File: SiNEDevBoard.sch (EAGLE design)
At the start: 37 parts, among them IC1 ATTINY24/44/84-SSU, IC2 74HC164D, J1 AVR_SPI_PRG_6NS

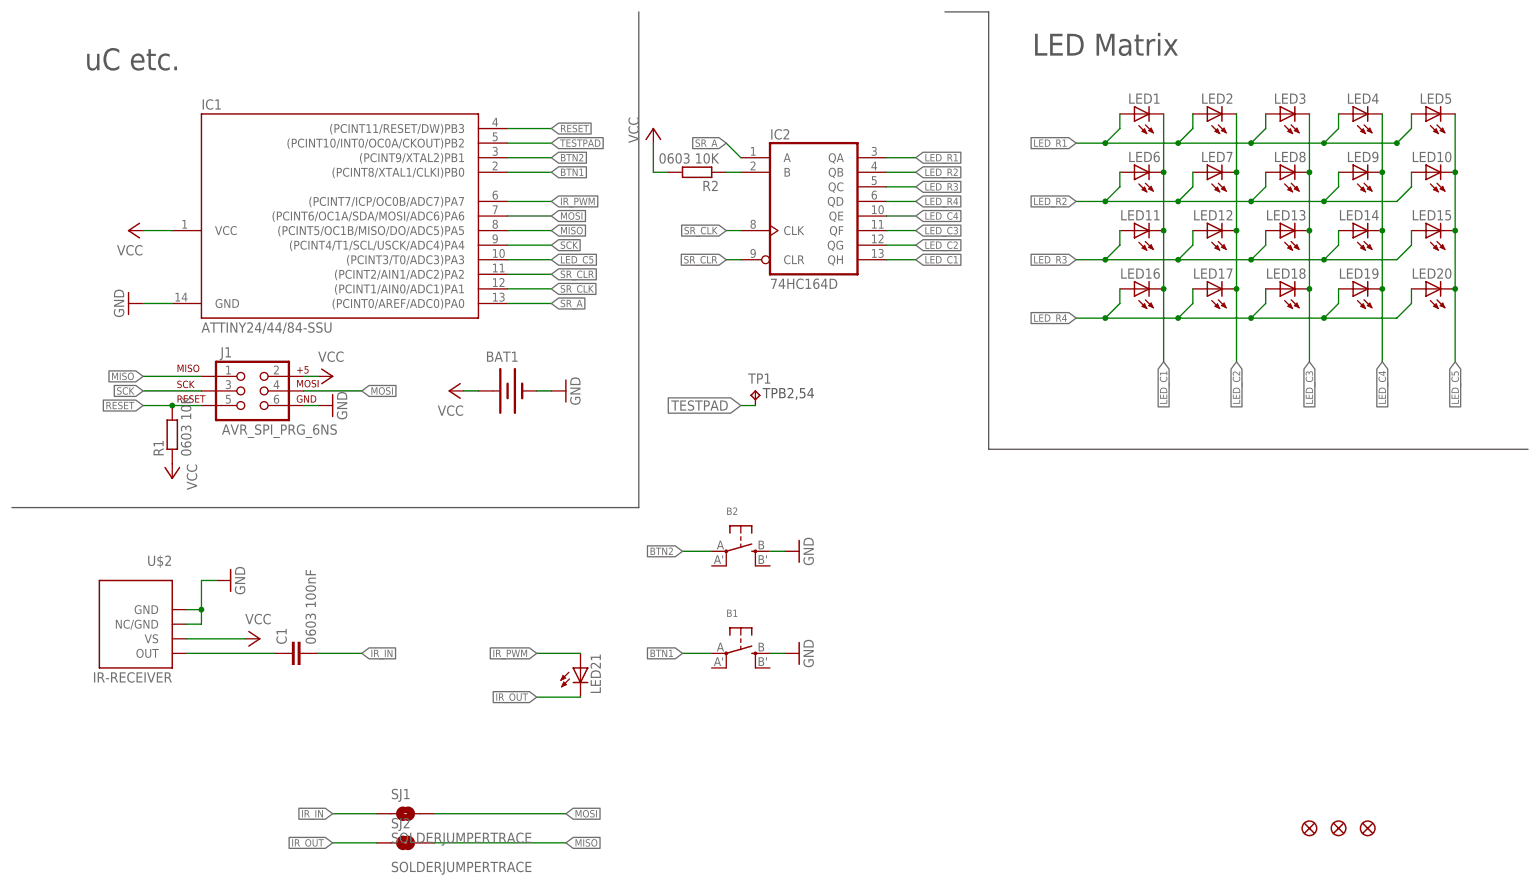
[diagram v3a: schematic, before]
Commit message: DevBoard V0.5 Final Changes including Teardrops, this version was sent to make 3 prototype boards
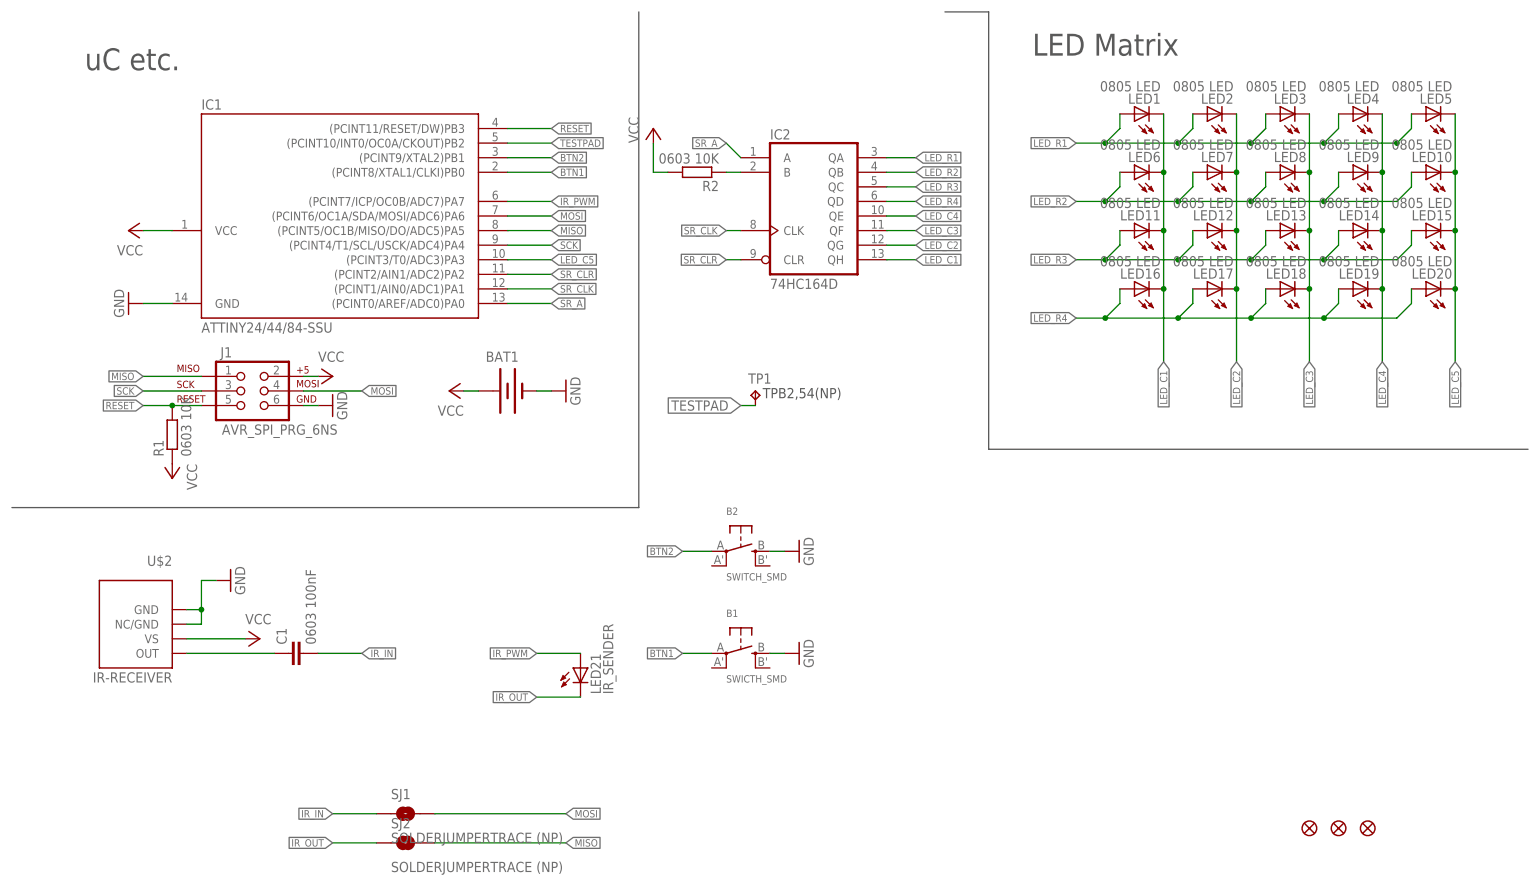
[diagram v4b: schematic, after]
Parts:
- B1: value (none) -> SWICTH_SMD
- B2: value (none) -> SWITCH_SMD
- LED1, LED10, LED11, LED12, LED13, LED14, LED15, LED16, LED17, LED18, LED19, LED2, LED20, LED3, LED4, LED5, LED6, LED7, LED8, LED9: value (none) -> 0805 LED
- LED21: value (none) -> IR_SENDER
- SJ1, SJ2: value SOLDERJUMPERTRACE -> SOLDERJUMPERTRACE (NP)
- TP1: value TPB2,54 -> TPB2,54(NP)
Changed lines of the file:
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@@
 <part name="GND3" library="supply1" deviceset="GND" device=""/>
 <part name="P+4" library="supply1" deviceset="VCC" device=""/>
-<part name="LED1" library="adafruit" deviceset="LED" device="CHIPLED_0805"/>
-<part name="LED2" library="adafruit" deviceset="LED" device="CHIPLED_0805"/>
-<part name="LED3" library="adafruit" deviceset="LED" device="CHIPLED_0805"/>
-<part name="LED4" library="adafruit" deviceset="LED" device="CHIPLED_0805"/>
-<part name="LED5" library="adafruit" deviceset="LED" device="CHIPLED_0805"/>
-<part name="LED6" library="adafruit" deviceset="LED" device="CHIPLED_0805"/>
-<part name="LED7" library="adafruit" deviceset="LED" device="CHIPLED_0805"/>
-<part name="LED8" library="adafruit" deviceset="LED" device="CHIPLED_0805"/>
-<part name="LED9" library="adafruit" deviceset="LED" device="CHIPLED_0805"/>
-<part name="LED10" library="adafruit" deviceset="LED" device="CHIPLED_0805"/>
-<part name="LED11" library="adafruit" deviceset="LED" device="CHIPLED_0805"/>
-<part name="LED12" library="adafruit" deviceset="LED" device="CHIPLED_0805"/>
-<part name="LED13" library="adafruit" deviceset="LED" device="CHIPLED_0805"/>
-<part name="LED14" library="adafruit" deviceset="LED" device="CHIPLED_0805"/>
-<part name="LED15" library="adafruit" deviceset="LED" device="CHIPLED_0805"/>
-<part name="LED16" library="adafruit" deviceset="LED" device="CHIPLED_0805"/>
-<part name="LED17" library="adafruit" deviceset="LED" device="CHIPLED_0805"/>
-<part name="LED18" library="adafruit" deviceset="LED" device="CHIPLED_0805"/>
-<part name="LED19" library="adafruit" deviceset="LED" device="CHIPLED_0805"/>
-<part name="LED20" library="adafruit" deviceset="LED" device="CHIPLED_0805"/>
+<part name="LED1" library="adafruit" deviceset="LED" device="CHIPLED_0805" value="0805 LED"/>
+<part name="LED2" library="adafruit" deviceset="LED" device="CHIPLED_0805" value="0805 LED"/>
+<part name="LED3" library="adafruit" deviceset="LED" device="CHIPLED_0805" value="0805 LED"/>
+<part name="LED4" library="adafruit" deviceset="LED" device="CHIPLED_0805" value="0805 LED"/>
+<part name="LED5" library="adafruit" deviceset="LED" device="CHIPLED_0805" value="0805 LED"/>
+<part name="LED6" library="adafruit" deviceset="LED" device="CHIPLED_0805" value="0805 LED"/>
+<part name="LED7" library="adafruit" deviceset="LED" device="CHIPLED_0805" value="0805 LED"/>
+<part name="LED8" library="adafruit" deviceset="LED" device="CHIPLED_0805" value="0805 LED"/>
+<part name="LED9" library="adafruit" deviceset="LED" device="CHIPLED_0805" value="0805 LED"/>
+<part name="LED10" library="adafruit" deviceset="LED" device="CHIPLED_0805" value="0805 LED"/>
+<part name="LED11" library="adafruit" deviceset="LED" device="CHIPLED_0805" value="0805 LED"/>
+<part name="LED12" library="adafruit" deviceset="LED" device="CHIPLED_0805" value="0805 LED"/>
+<part name="LED13" library="adafruit" deviceset="LED" device="CHIPLED_0805" value="0805 LED"/>
+<part name="LED14" library="adafruit" deviceset="LED" device="CHIPLED_0805" value="0805 LED"/>
+<part name="LED15" library="adafruit" deviceset="LED" device="CHIPLED_0805" value="0805 LED"/>
+<part name="LED16" library="adafruit" deviceset="LED" device="CHIPLED_0805" value="0805 LED"/>
+<part name="LED17" library="adafruit" deviceset="LED" device="CHIPLED_0805" value="0805 LED"/>
+<part name="LED18" library="adafruit" deviceset="LED" device="CHIPLED_0805" value="0805 LED"/>
+<part name="LED19" library="adafruit" deviceset="LED" device="CHIPLED_0805" value="0805 LED"/>
+<part name="LED20" library="adafruit" deviceset="LED" device="CHIPLED_0805" value="0805 LED"/>
 <part name="FRAME1" library="frames" deviceset="DINA4_L" device=""/>
 <part name="IC2" library="74xx-eu" deviceset="74*164" device="D" technology="HC"/>
@@
 <part name="P+6" library="supply1" deviceset="VCC" device=""/>
 <part name="C1" library="rcl" deviceset="C-EU" device="C0805" value="0603 100nF"/>
-<part name="LED21" library="led" deviceset="LED" device="CHIPLED_1206"/>
-<part name="B1" library="microbuilder" deviceset="SWITCH_TACT_SMT" device=""/>
-<part name="B2" library="microbuilder" deviceset="SWITCH_TACT_SMT" device=""/>
+<part name="LED21" library="led" deviceset="LED" device="CHIPLED_1206" value="IR_SENDER"/>
+<part name="B1" library="microbuilder" deviceset="SWITCH_TACT_SMT" device="" value="SWICTH_SMD"/>
+<part name="B2" library="microbuilder" deviceset="SWITCH_TACT_SMT" device="" value="SWITCH_SMD"/>
 <part name="GND5" library="supply1" deviceset="GND" device=""/>
 <part name="GND6" library="supply1" deviceset="GND" device=""/>
-<part name="SJ1" library="SparkFun" deviceset="SOLDERJUMPER" device="TRACE"/>
-<part name="SJ2" library="SparkFun" deviceset="SOLDERJUMPER" device="TRACE"/>
+<part name="SJ1" library="SparkFun" deviceset="SOLDERJUMPER" device="TRACE" value="SOLDERJUMPERTRACE (NP)"/>
+<part name="SJ2" library="SparkFun" deviceset="SOLDERJUMPER" device="TRACE" value="SOLDERJUMPERTRACE (NP)"/>
 <part name="JP1" library="CISECO eaglecad designs" deviceset="FIDUCIAL" device="1X2.5-STOP"/>
 <part name="JP2" library="CISECO eaglecad designs" deviceset="FIDUCIAL" device="1X2.5-STOP"/>
@@
 <part name="U$2" library="CISECO eaglecad designs" deviceset="IR-RECEIVER" device=""/>
 <part name="GND7" library="supply1" deviceset="GND" device=""/>
-<part name="TP1" library="CISECO eaglecad designs" deviceset="TP" device="B2,54"/>
+<part name="TP1" library="CISECO eaglecad designs" deviceset="TP" device="B2,54" value="TPB2,54(NP)"/>
 </parts>
 <sheets>

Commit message: Added parts use in DevBoard v0.5 to the lbr Update parts in the DevBoard to use versions from the lbr DevBoard V0.5a
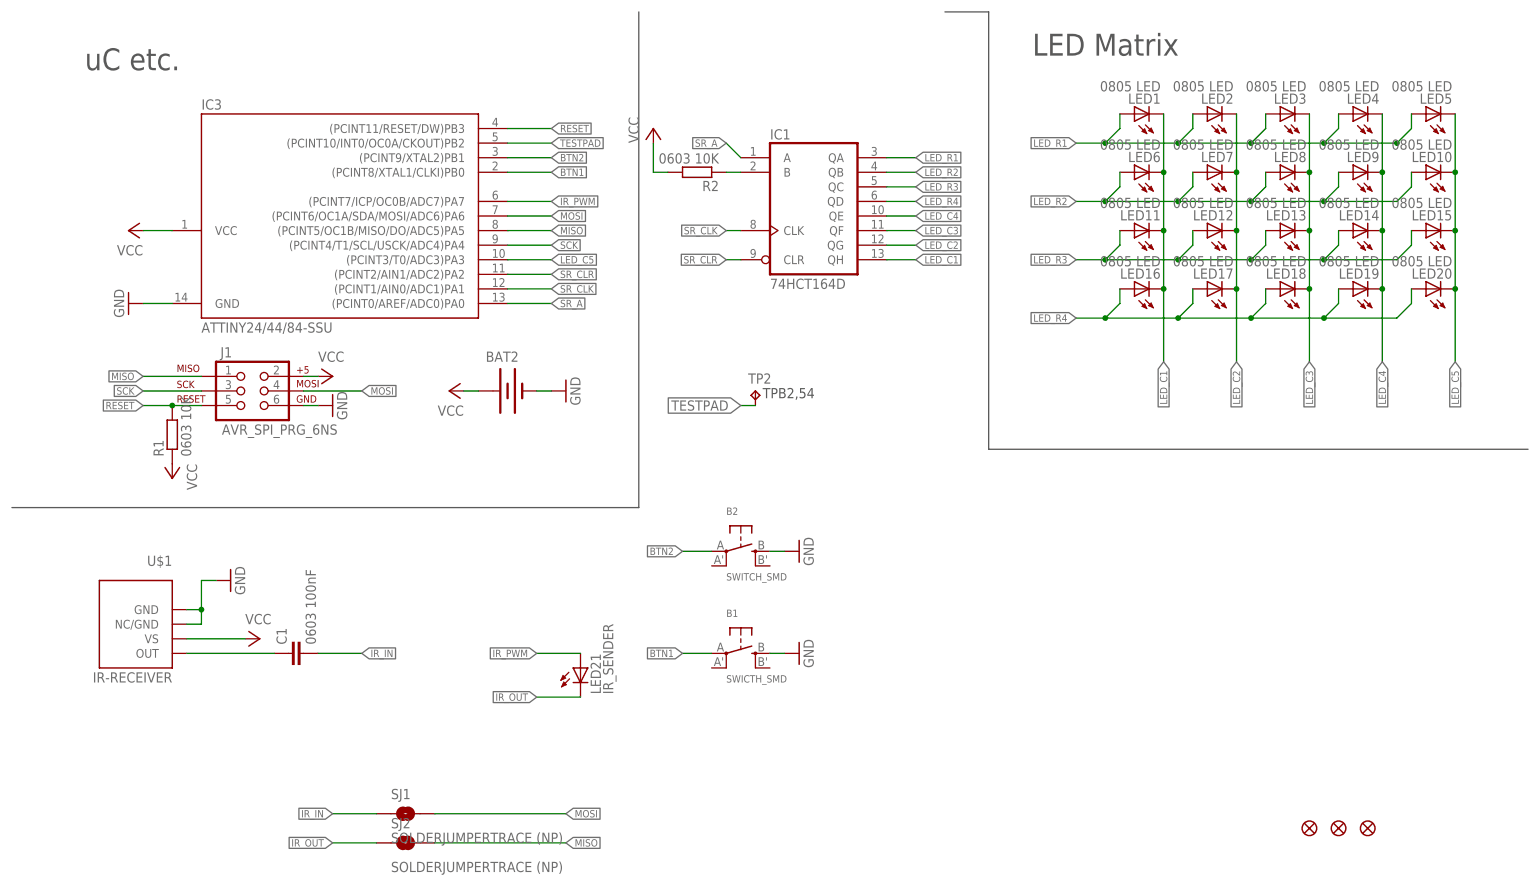
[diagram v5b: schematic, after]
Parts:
- removed BAT1: (no value), SparkFun:BATTERY20SMD
- removed IC2: 74HC164D, 74xx-eu:74HC164D
- removed TP1: TPB2,54(NP), CISECO eaglecad designs:TPB2,54
- removed U$2: IR-RECEIVER, CISECO eaglecad designs:IR-RECEIVER
- added BAT2: (no value), SiNE Parts:BATTERY20SMD
- added IC3: ATTINY24/44/84-SSU, SiNE Parts:ATTINY24/44/84-SSU
- added TP2: TPB2,54, SiNE Parts:TPB2,54
- added U$1: IR-RECEIVER, SiNE Parts:IR-RECEIVER
- IC1: value ATTINY24/44/84-SSU -> 74HCT164D; device attiny24_44_84:ATTINY24/44/84-SSU -> SiNE Parts:74HCT164D
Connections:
- net BTN1: now also IC3.(PCINT8/XTAL1/CLKI)PB0; no longer IC1.(PCINT8/XTAL1/CLKI)PB0
- net BTN2: now also IC3.(PCINT9/XTAL2)PB1; no longer IC1.(PCINT9/XTAL2)PB1
- net GND: now also BAT2.-, IC3.GND, U$1.GND, U$1.NC/GND; no longer BAT1.-, IC1.GND, U$2.GND, U$2.NC/GND
- net IR_PWM: now also IC3.(PCINT7/ICP/OC0B/ADC7)PA7; no longer IC1.(PCINT7/ICP/OC0B/ADC7)PA7
- net LED_C1: now also IC1A.QH; no longer IC2A.QH
- net LED_C2: now also IC1A.QG; no longer IC2A.QG
- net LED_C3: now also IC1A.QF; no longer IC2A.QF
- net LED_C4: now also IC1A.QE; no longer IC2A.QE
- net LED_C5: now also IC3.(PCINT3/T0/ADC3)PA3; no longer IC1.(PCINT3/T0/ADC3)PA3
- net LED_R1: now also IC1A.QA; no longer IC2A.QA
- net LED_R2: now also IC1A.QB; no longer IC2A.QB
- net LED_R3: now also IC1A.QC; no longer IC2A.QC
- net LED_R4: now also IC1A.QD; no longer IC2A.QD
- net MISO: now also IC3.(PCINT5/OC1B/MISO/DO/ADC5)PA5; no longer IC1.(PCINT5/OC1B/MISO/DO/ADC5)PA5
- net MOSI: now also IC3.(PCINT6/OC1A/SDA/MOSI/ADC6)PA6; no longer IC1.(PCINT6/OC1A/SDA/MOSI/ADC6)PA6
- net N$1: now also IC1A.B; no longer IC2A.B
- net N$6: now also U$1.OUT; no longer U$2.OUT
- net RESET: now also IC3.(PCINT11/RESET/DW)PB3; no longer IC1.(PCINT11/RESET/DW)PB3
- net SCK: now also IC3.(PCINT4/T1/SCL/USCK/ADC4)PA4; no longer IC1.(PCINT4/T1/SCL/USCK/ADC4)PA4
- net SR_A: now also IC1A.A, IC3.(PCINT0/AREF/ADC0)PA0; no longer IC1.(PCINT0/AREF/ADC0)PA0, IC2A.A
- net SR_CLK: now also IC1A.CLK, IC3.(PCINT1/AIN0/ADC1)PA1; no longer IC1.(PCINT1/AIN0/ADC1)PA1, IC2A.CLK
- net SR_CLR: now also IC1A.CLR, IC3.(PCINT2/AIN1/ADC2)PA2; no longer IC1.(PCINT2/AIN1/ADC2)PA2, IC2A.CLR
- net TESTPAD: now also IC3.(PCINT10/INT0/OC0A/CKOUT)PB2, TP2.TP; no longer IC1.(PCINT10/INT0/OC0A/CKOUT)PB2, TP1.TP
- net VCC: now also BAT2.+, IC3.VCC, U$1.VS; no longer BAT1.+, IC1.VCC, U$2.VS
